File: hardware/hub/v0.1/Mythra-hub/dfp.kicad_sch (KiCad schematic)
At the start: 42 parts, among them J3 918-418K2022C40000, J7 DFP SWD, Q1 Q_NMOS_GSD, U12 DAC5311xDCK, U16 CYPD3174-24, U23 TPD4E02B04DQA, U24 TPD4E02B04DQA, U31 SP3400-02UTG, U4 HD3SS460, U8 SiC437/8

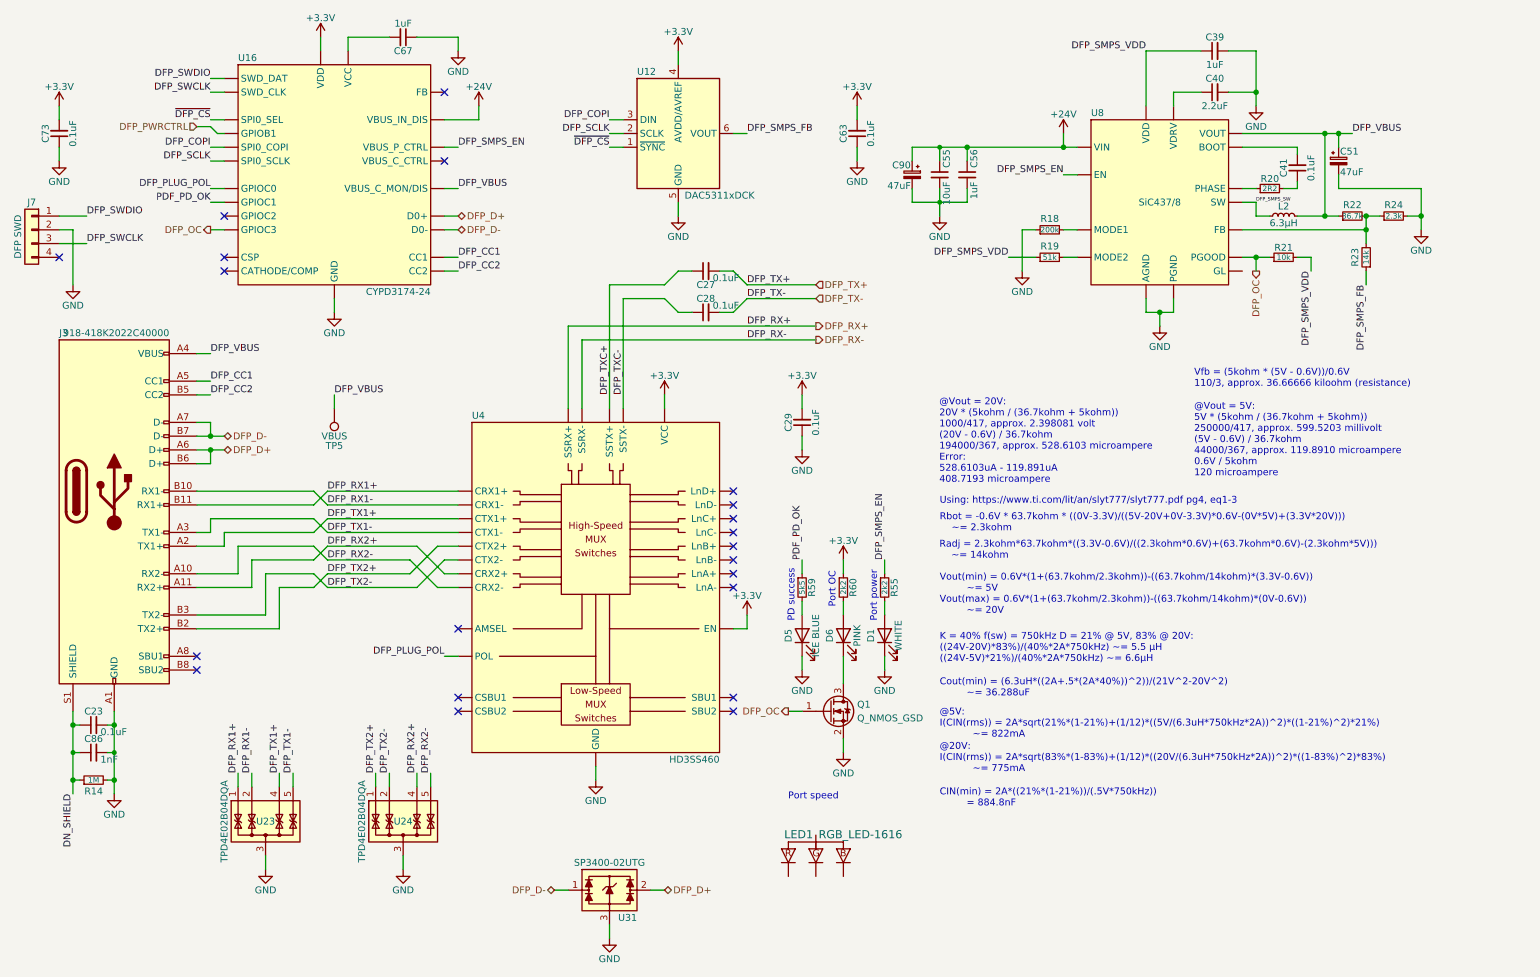
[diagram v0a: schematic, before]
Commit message: Cleaned up from adding the indicators
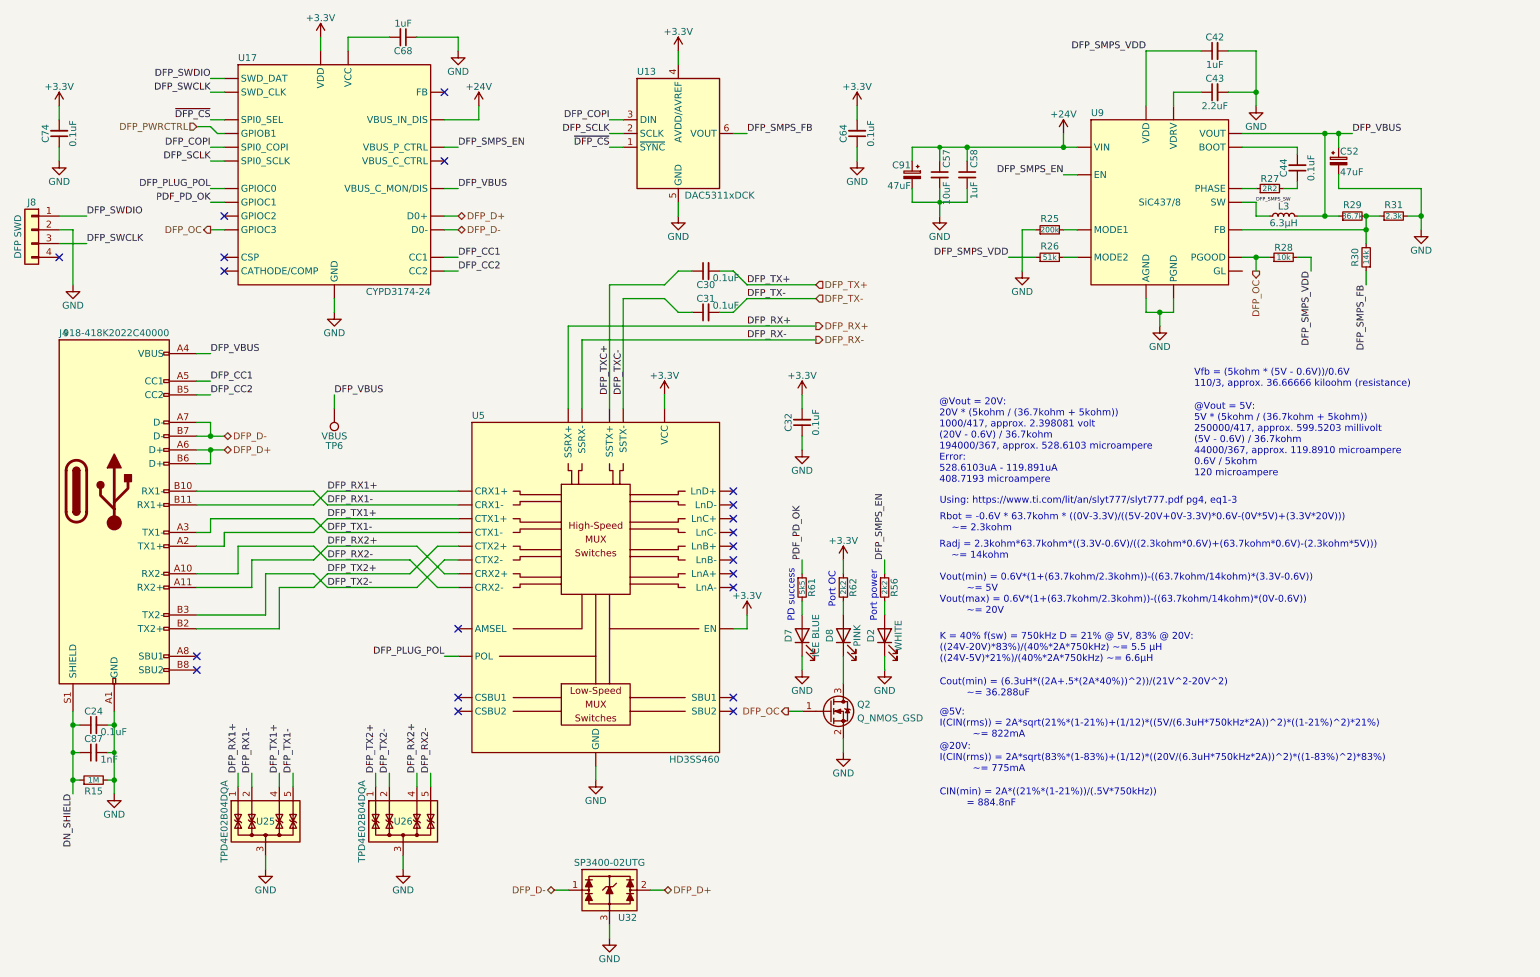
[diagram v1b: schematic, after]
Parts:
- removed LED1: RGB_LED-1616, rhais_led:LED0606_Clockwise, symbol DX_MON:RGB_LED-1616
- renumbered C23 to C24, C27 to C30, C28 to C31, C29 to C32, C39 to C42, C40 to C43, C41 to C44, C51 to C52, C55 to C57, C56 to C58, C63 to C64, C67 to C68, C73 to C74, C86 to C87, C90 to C91, D1 to D2, D5 to D7, D6 to D8, J3 to J4, J7 to J8, L2 to L3, Q1 to Q2, R14 to R15, R18 to R25, R19 to R26, R20 to R27, R21 to R28, R22 to R29, R23 to R30, R24 to R31, R55 to R56, R59 to R61, R60 to R62, TP5 to TP6, U12 to U13, U16 to U17, U23 to U25, U24 to U26, U31 to U32, U4 to U5, U8 to U9
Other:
- note removed: "Port speed"

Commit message: Finished working through the fab checklists
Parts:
- renumbered C24 to C23, C30 to C27, C31 to C28, C32 to C29, C42 to C39, C43 to C40, C44 to C41, C52 to C51, C57 to C55, C58 to C56, C64 to C63, C68 to C67, C74 to C73, C87 to C86, C91 to C90, D2 to D1, D7 to D5, D8 to D6, J4 to J3, J8 to J7, L3 to L2, Q2 to Q1, R15 to R14, R25 to R18, R26 to R19, R27 to R20, R28 to R21, R29 to R22, R30 to R23, R31 to R24, R56 to R55, R61 to R59, R62 to R60, TP6 to TP5, U13 to U12, U17 to U16, U25 to U23, U26 to U24, U32 to U31, U5 to U4, U9 to U8

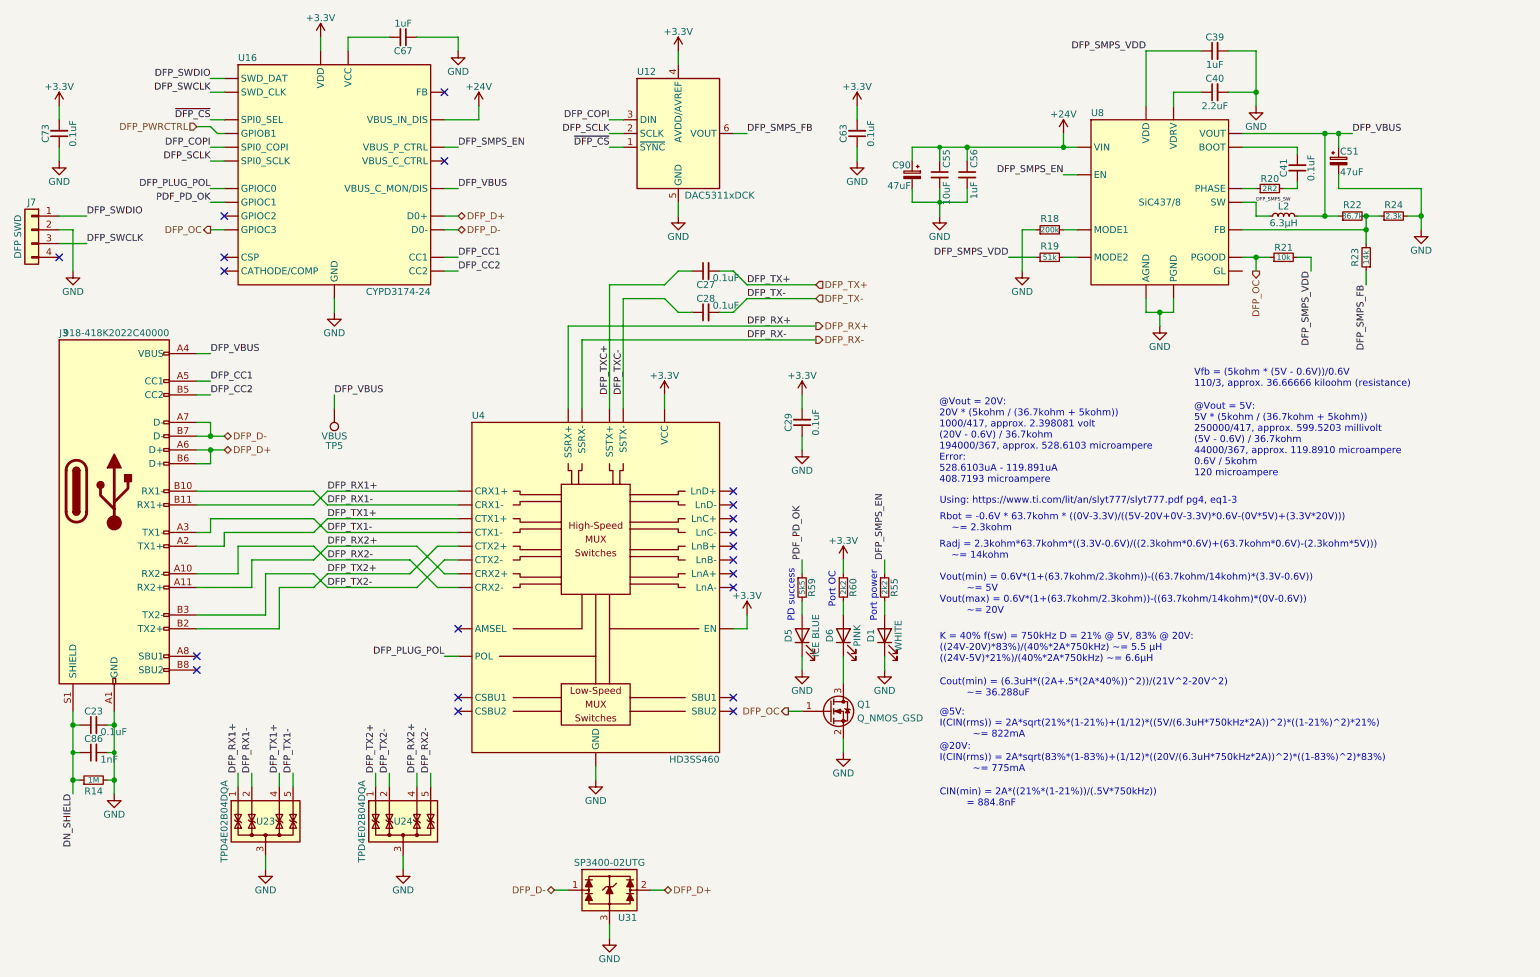
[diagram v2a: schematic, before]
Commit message: Upgraded the schematic files to KiCad 6 format and done some tidy up from the manufacturing crunch
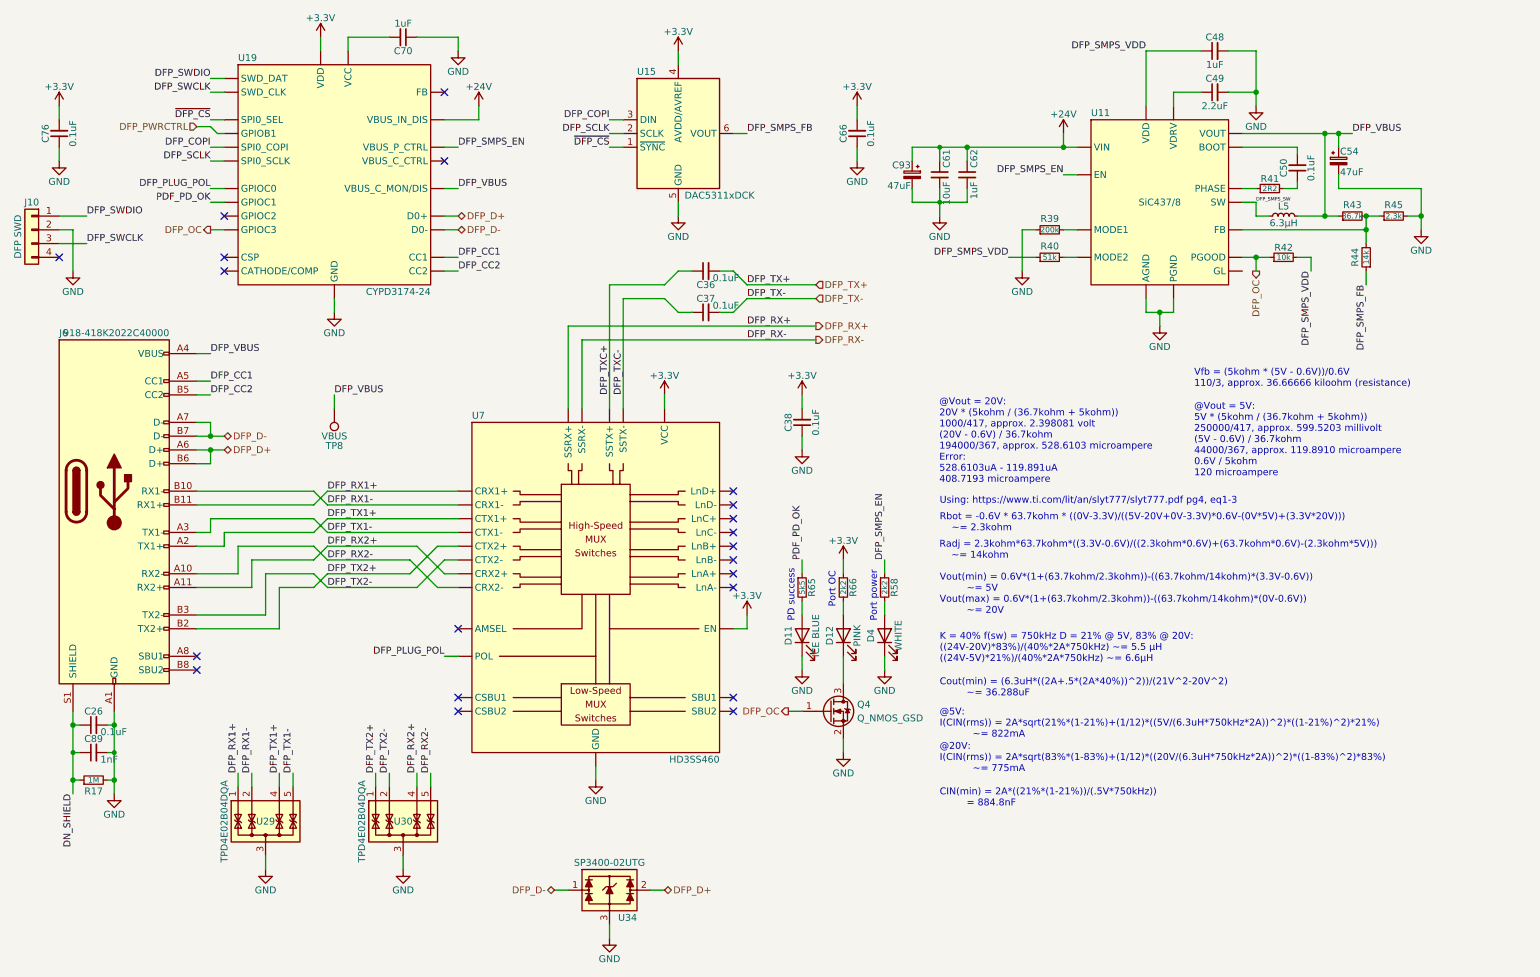
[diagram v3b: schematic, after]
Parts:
- C89: renamed from C86; MFR Yageo -> Walsin; MPN RC0402FR-0710KL -> 0402B102K500CT; OC_FARNELL (none) -> 2496767; OC_LCSC C60490 -> (none); URL_FARNELL (none) -> https://uk.farnell.com/walsin/0402b102k500ct/cap-1000pf-50v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; URL_LCSC https://www.lcsc.com/product-detail/Chip-Resistor-Surface-M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 -> (none)
- R58: renamed from R55; MPN MCWR04W2R20FTL -> MCWR04X2201FTL; OC_FARNELL 2447154 -> 2447148; URL_FARNELL https://uk.farnell.com/multicomp/mcwr04w2r20ftl/res-2r2-1-0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 -> https://uk.farnell.com/multicomp/mcwr04x2201ftl/res-2k2-1-0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
- R65: renamed from R59; MPN MCWR04W2R20FTL -> MCWR04X5601FTL; OC_FARNELL 2447154 -> 2447202; URL_FARNELL https://uk.farnell.com/multicomp/mcwr04w2r20ftl/res-2r2-1-0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 -> https://uk.farnell.com/multicomp/mcwr04x5601ftl/res-5k6-1-0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
- R66: renamed from R60; MPN MCWR04W2R20FTL -> MCWR04X2201FTL; OC_FARNELL 2447154 -> 2447148; URL_FARNELL https://uk.farnell.com/multicomp/mcwr04w2r20ftl/res-2r2-1-0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 -> https://uk.farnell.com/multicomp/mcwr04x2201ftl/res-2k2-1-0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
- renumbered C23 to C26, C27 to C36, C28 to C37, C29 to C38, C39 to C48, C40 to C49, C41 to C50, C51 to C54, C55 to C61, C56 to C62, C63 to C66, C67 to C70, C73 to C76, C90 to C93, D5 to D11, D6 to D12, D1 to D4, J7 to J10, J3 to J6, L2 to L5, Q1 to Q4, R14 to R17, R18 to R39, R19 to R40, R20 to R41, R21 to R42, R22 to R43, R23 to R44, R24 to R45, TP5 to TP8, U8 to U11, U12 to U15, U16 to U19, U23 to U29, U24 to U30, U31 to U34, U4 to U7

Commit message: Fixed the PD controller footprints so the gnd on pin 22 was hooked up
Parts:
- U19: MFR Cypress -> (property "Reference" "U" (id 0) (at -17.78 21.59 0); MPN CYPD3174-24LQXQ -> (effects (font (size 1.27 1.27)) (justify left)); OC_FARNELL 2896248 -> ); URL_FARNELL https://uk.farnell.com/cypress-semiconductor/cypd3174-24lqx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 -> (property "Value" "CYPD3174-24" (id 1) (at 17.78 -21.59 0)
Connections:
- net GND: now also U19.22 (GND)

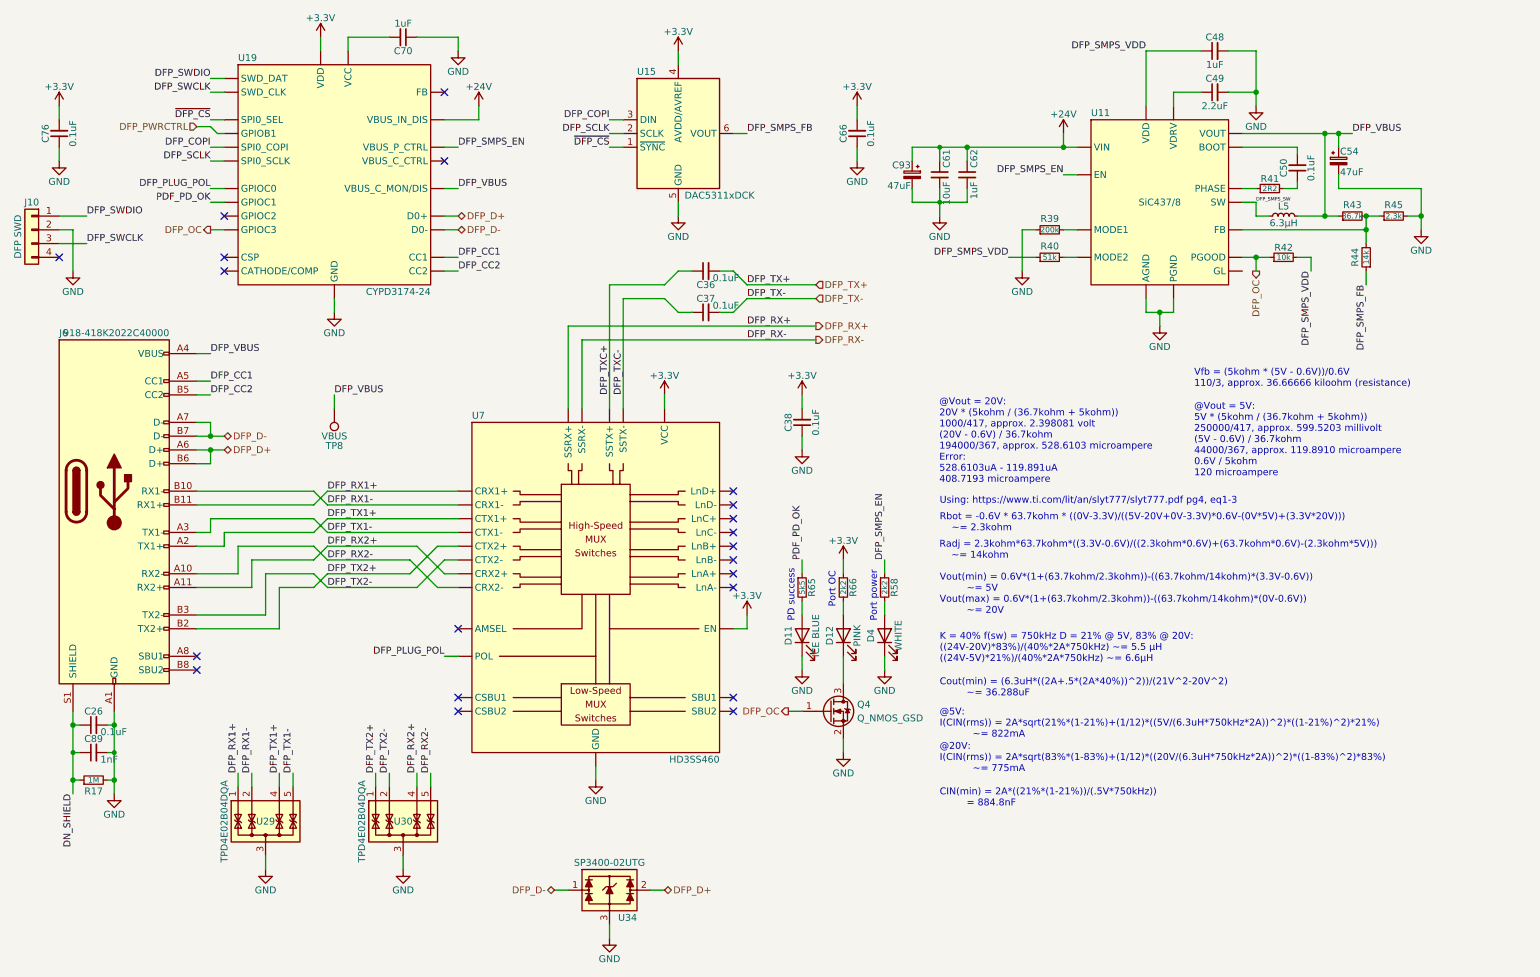
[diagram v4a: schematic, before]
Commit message: Fixed some mishaps with the PD controller metadata fields and sync'd the schematic and PCB for the hub
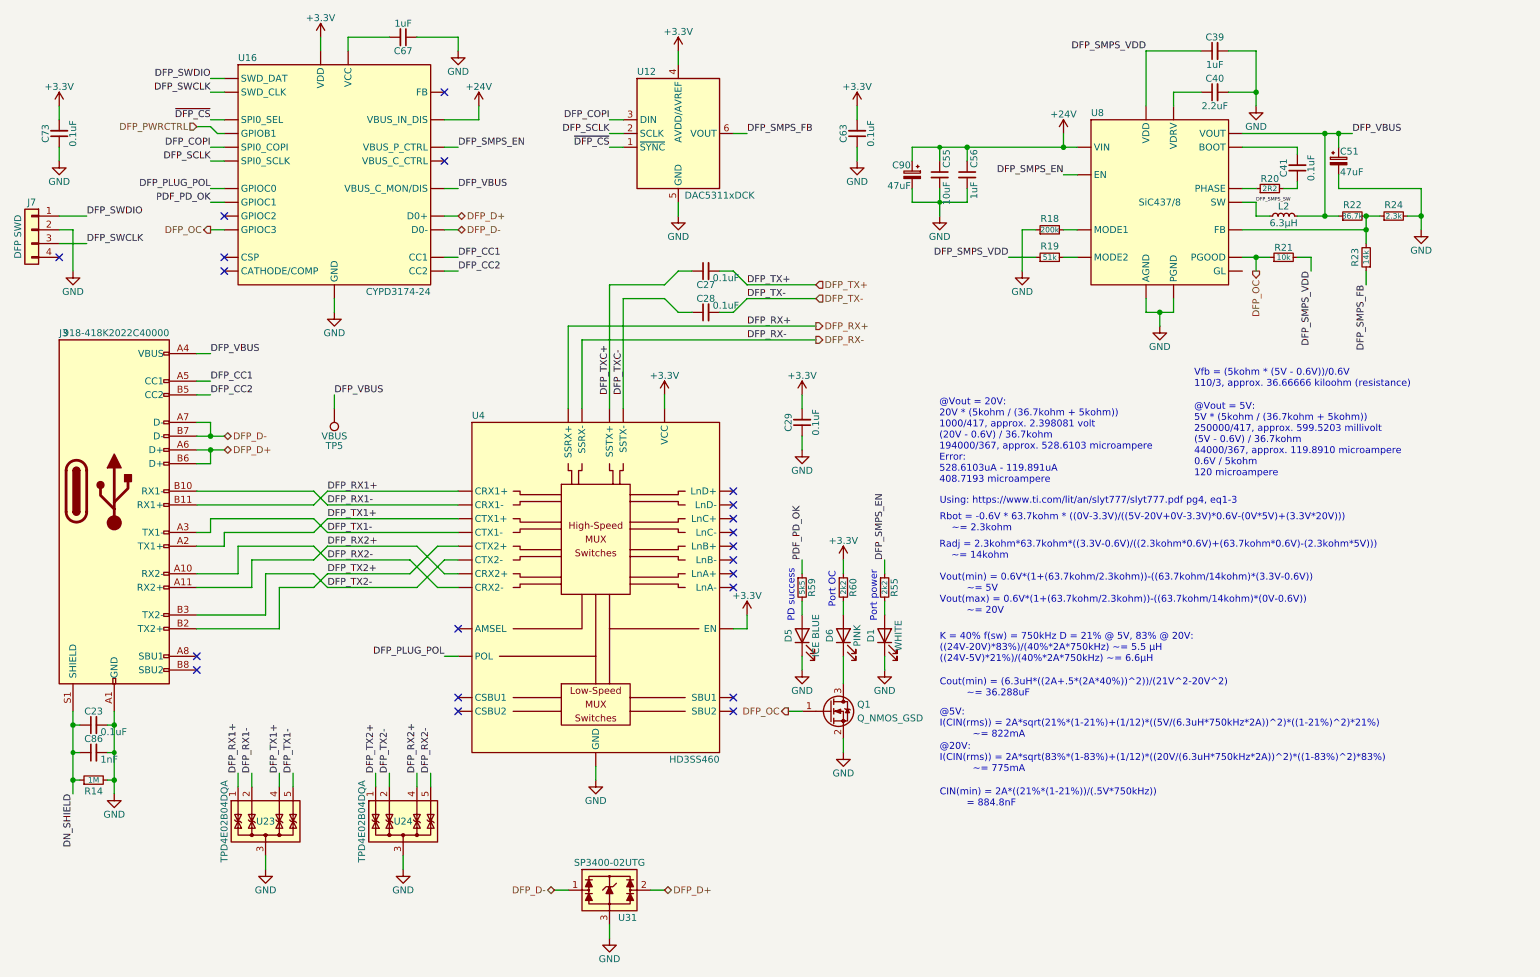
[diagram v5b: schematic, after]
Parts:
- U16: renamed from U19; MFR (property "Reference" "U" (id 0) (at -17.78 21.59 0) -> Cypress; MPN (effects (font (size 1.27 1.27)) (justify left)) -> CYPD3174-24LQXQ; OC_FARNELL ) -> 2896248; URL_FARNELL (property "Value" "CYPD3174-24" (id 1) (at 17.78 -21.59 0) -> https://uk.farnell.com/cypress-semiconductor/cypd3174-24lqx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
- renumbered C26 to C23, C36 to C27, C37 to C28, C38 to C29, C48 to C39, C49 to C40, C50 to C41, C54 to C51, C61 to C55, C62 to C56, C66 to C63, C70 to C67, C76 to C73, C89 to C86, C93 to C90, D4 to D1, D11 to D5, D12 to D6, J6 to J3, J10 to J7, L5 to L2, Q4 to Q1, R17 to R14, R39 to R18, R40 to R19, R41 to R20, R42 to R21, R43 to R22, R44 to R23, R45 to R24, R58 to R55, R65 to R59, R66 to R60, TP8 to TP5, U15 to U12, U29 to U23, U30 to U24, U34 to U31, U7 to U4, U11 to U8
